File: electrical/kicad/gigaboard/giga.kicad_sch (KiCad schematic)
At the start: 50 parts, among them J1 Conn_02x03_Counter_Clockwise, J10 Conn_01x04, J11 Conn_01x04, J12 Conn_01x04, J13 Conn_01x04, J14 Conn_01x04, J15 Conn_01x04, J16 Conn_01x04, J17 Conn_01x04, J18 Conn_01x04, J19 Conn_01x04, J2 Conn_02x04_Counter_Clockwise, J20 Conn_01x04, J21 Conn_01x04, J22 Screw_Terminal_01x03, J23 Conn_02x12_Counter_Clockwise, J3 Conn_02x04_Counter_Clockwise, J4 Conn_02x04_Counter_Clockwise, J5 Conn_02x04_Counter_Clockwise, J6 Conn_02x04_Counter_Clockwise, J7 Conn_01x04, J8 Conn_01x04, J9 Conn_01x04, U1 TMC2209, U2 TMC2209, U3 TMC2209, U4 TMC2209, U5 TMC2209, U6 TMC2209

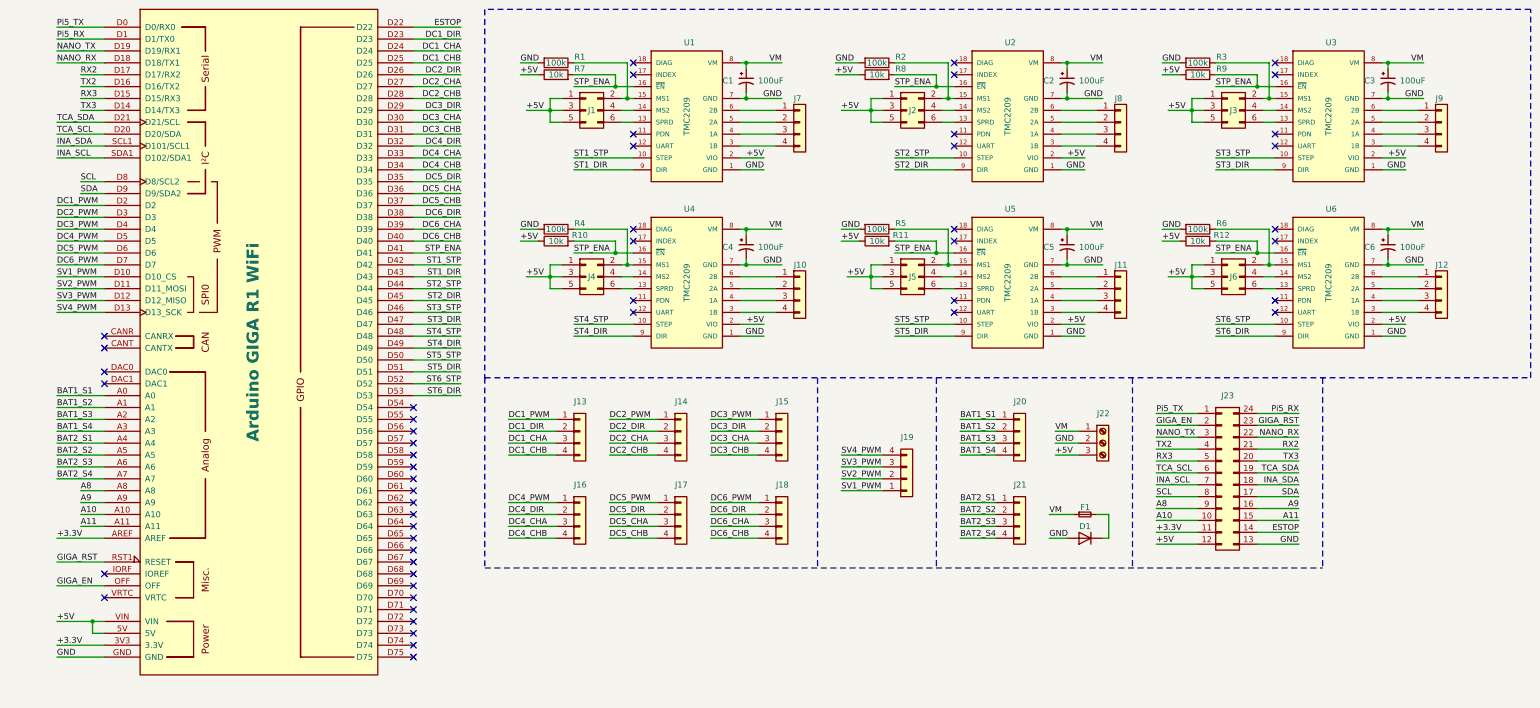
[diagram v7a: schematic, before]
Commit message: update(giga): pcb wiring complete (DRC passed)
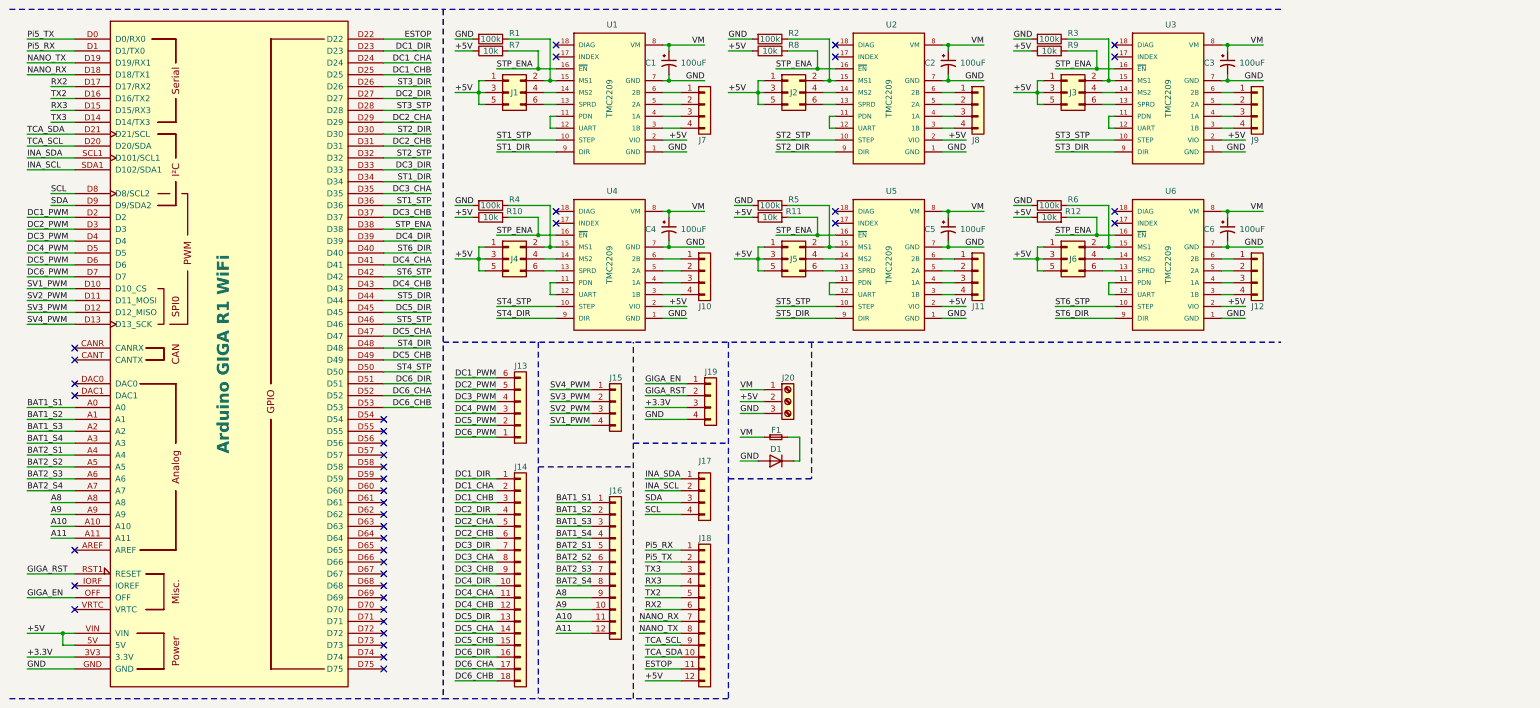
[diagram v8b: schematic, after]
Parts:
- removed J13, J14, J15, J16, J18, J20, J21: Conn_01x04, Connector_PinHeader_2.54mm:PinHeader_1x04_P2.54mm_Vertical, symbol Connector_Generic:Conn_01x04
- removed J23: Conn_02x12_Counter_Clockwise, Connector_PinHeader_2.54mm:PinHeader_2x12_P2.54mm_Vertical, symbol Connector_Generic:Conn_02x12_Counter_Clockwise
- added J13: Conn_01x06, Connector_PinHeader_2.54mm:PinHeader_1x06_P2.54mm_Vertical, symbol Connector_Generic:Conn_01x06
- added J14: Conn_01x18, Connector_PinHeader_2.54mm:PinHeader_1x18_P2.54mm_Vertical, symbol Connector_Generic:Conn_01x18
- added J16, J18: Conn_01x12, Connector_PinHeader_2.54mm:PinHeader_1x12_P2.54mm_Vertical, symbol Connector_Generic:Conn_01x12
- added J19: Conn_01x04, Connector_PinHeader_2.54mm:PinHeader_1x04_P2.54mm_Vertical, symbol Connector_Generic:Conn_01x04
- renumbered J19 to J15, J22 to J20
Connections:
- net +3.3V: now also J19.3 (Pin_3); no longer A1.AREF
- net +5V: now also J20.2 (Pin_2), J18.12 (Pin_12); no longer J20.3 (Pin_3)
- net A10: now also J16.11 (Pin_11)
- net A11: now also J16.12 (Pin_12)
- net A8: now also J16.9 (Pin_9)
- net A9: now also J16.10 (Pin_10)
- net BAT1_S1: now also J16.1 (Pin_1)
- net BAT1_S2: now also J16.2 (Pin_2)
- net BAT1_S3: now also J16.3 (Pin_3)
- net BAT1_S4: now also J16.4 (Pin_4)
- net BAT2_S1: now also J16.5 (Pin_5)
- net BAT2_S2: now also J16.6 (Pin_6)
- net BAT2_S3: now also J16.7 (Pin_7)
- net BAT2_S4: now also J16.8 (Pin_8)
- net DC1_CHA: now also J14.2 (Pin_2)
- net DC1_CHB: now also J14.3 (Pin_3)
- net DC1_DIR: now also J14.1 (Pin_1)
- net DC1_PWM: now also J13.6 (Pin_6)
- net DC2_CHA: now also A1.D29, J14.5 (Pin_5); no longer A1.D27
- net DC2_CHB: now also A1.D31, J14.6 (Pin_6); no longer A1.D28
- net DC2_DIR: now also A1.D27, J14.4 (Pin_4); no longer A1.D26
- net DC2_PWM: now also J13.5 (Pin_5)
- net DC3_CHA: now also A1.D35, J14.8 (Pin_8); no longer A1.D30
- net DC3_CHB: now also A1.D37, J14.9 (Pin_9); no longer A1.D31
- net DC3_DIR: now also A1.D33, J14.7 (Pin_7); no longer A1.D29
- net DC3_PWM: now also J13.4 (Pin_4)
- net DC4_CHA: now also A1.D41, J14.11 (Pin_11); no longer A1.D33
- net DC4_CHB: now also A1.D43, J14.12 (Pin_12); no longer A1.D34
- net DC4_DIR: now also A1.D39, J14.10 (Pin_10); no longer A1.D32
- net DC4_PWM: now also J13.3 (Pin_3)
- net DC5_CHA: now also A1.D47, J14.14 (Pin_14); no longer A1.D36, J17.3 (Pin_3)
- net DC5_CHB: now also A1.D49, J14.15 (Pin_15); no longer A1.D37, J17.4 (Pin_4)
- net DC5_DIR: now also A1.D45, J14.13 (Pin_13); no longer A1.D35, J17.2 (Pin_2)
- net DC5_PWM: now also J13.2 (Pin_2); no longer J17.1 (Pin_1)
- net DC6_CHA: now also A1.D52, J14.17 (Pin_17); no longer A1.D39
- net DC6_CHB: now also A1.D53, J14.18 (Pin_18); no longer A1.D40
- net DC6_DIR: now also A1.D51, J14.16 (Pin_16); no longer A1.D38
- net DC6_PWM: now also J13.1 (Pin_1)
- net ESTOP: now also J18.11 (Pin_11)
- net GIGA_EN: now also J19.1 (Pin_1)
- net GIGA_RST: now also J19.2 (Pin_2)
- net GND: now also J20.3 (Pin_3), J19.4 (Pin_4); no longer J20.2 (Pin_2)
- net INA_SCL: now also J17.2 (Pin_2)
- net INA_SDA: now also J17.1 (Pin_1)
- net NANO_RX: now also J18.7 (Pin_7)
- net NANO_TX: now also J18.8 (Pin_8)
- net Pi5_RX: now also J18.1 (Pin_1)
- net Pi5_TX: now also J18.2 (Pin_2)
- net RX2: now also J18.6 (Pin_6)
- net RX3: now also J18.4 (Pin_4)
- net SCL: now also J17.4 (Pin_4)
- net SDA: now also J17.3 (Pin_3)
- net ST1_DIR: now also A1.D34; no longer A1.D43
- net ST1_STP: now also A1.D36; no longer A1.D42
- net ST2_DIR: now also A1.D30; no longer A1.D45
- net ST2_STP: now also A1.D32; no longer A1.D44
- net ST3_DIR: now also A1.D26; no longer A1.D47
- net ST3_STP: now also A1.D28; no longer A1.D46
- net ST4_DIR: now also A1.D48; no longer A1.D49
- net ST4_STP: now also A1.D50; no longer A1.D48
- net ST5_DIR: now also A1.D44; no longer A1.D51
- net ST5_STP: now also A1.D46; no longer A1.D50
- net ST6_DIR: now also A1.D40; no longer A1.D53
- net ST6_STP: now also A1.D42; no longer A1.D52
- net STP_ENA: now also A1.D38; no longer A1.D41
- net SV1_PWM: now also J15.4 (Pin_4); no longer J15.1 (Pin_1)
- net SV2_PWM: now also J15.3 (Pin_3); no longer J15.2 (Pin_2)
- net SV3_PWM: now also J15.2 (Pin_2); no longer J15.3 (Pin_3)
- net SV4_PWM: now also J15.1 (Pin_1); no longer J15.4 (Pin_4)
- net TCA_SCL: now also J18.9 (Pin_9)
- net TCA_SDA: now also J18.10 (Pin_10)
- net TX2: now also J18.5 (Pin_5)
- net TX3: now also J18.3 (Pin_3)
- net at U3.11 (PDN): now also U3.12 (UART)
- net at U4.11 (PDN): now also U4.12 (UART)
- net at U2.11 (PDN): now also U2.12 (UART)
- net at U5.11 (PDN): now also U5.12 (UART)
- net at U6.11 (PDN): now also U6.12 (UART)
- net at U1.11 (PDN): now also U1.12 (UART)
- no-connect marks 52 -> 41
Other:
- company: (none) -> Team RED
- title: (none) -> Giga Board
- moved on the sheet: C1, C2, C3, C4, C5, C6, J1, J10, J11, J12, J15, J2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
